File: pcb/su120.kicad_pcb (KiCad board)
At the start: 2 copper layers, 94.1 x 94.1 mm, 293 parts, among them SW1 SW_Push, SW10 SW_Push, SW11 SW_Push, SW12 SW_Push, SW13 SW_Push, SW14 SW_Push, SW15 SW_Push, SW2 SW_Push, SW3 SW_Push, SW4 SW_Push, SW5 SW_Push, SW6 SW_Push, SW7 SW_Push, SW8 SW_Push, SW9 SW_Push

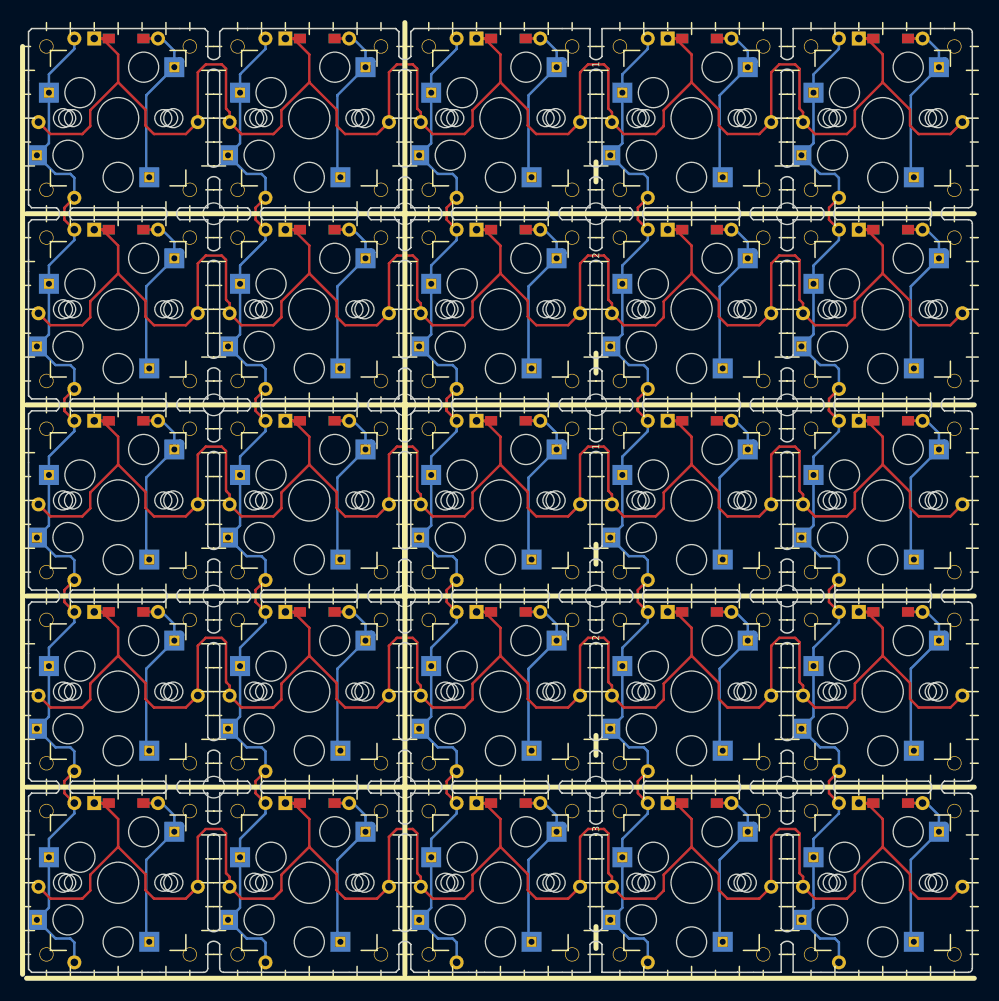
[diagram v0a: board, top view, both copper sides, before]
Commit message: modify to fit choc v2
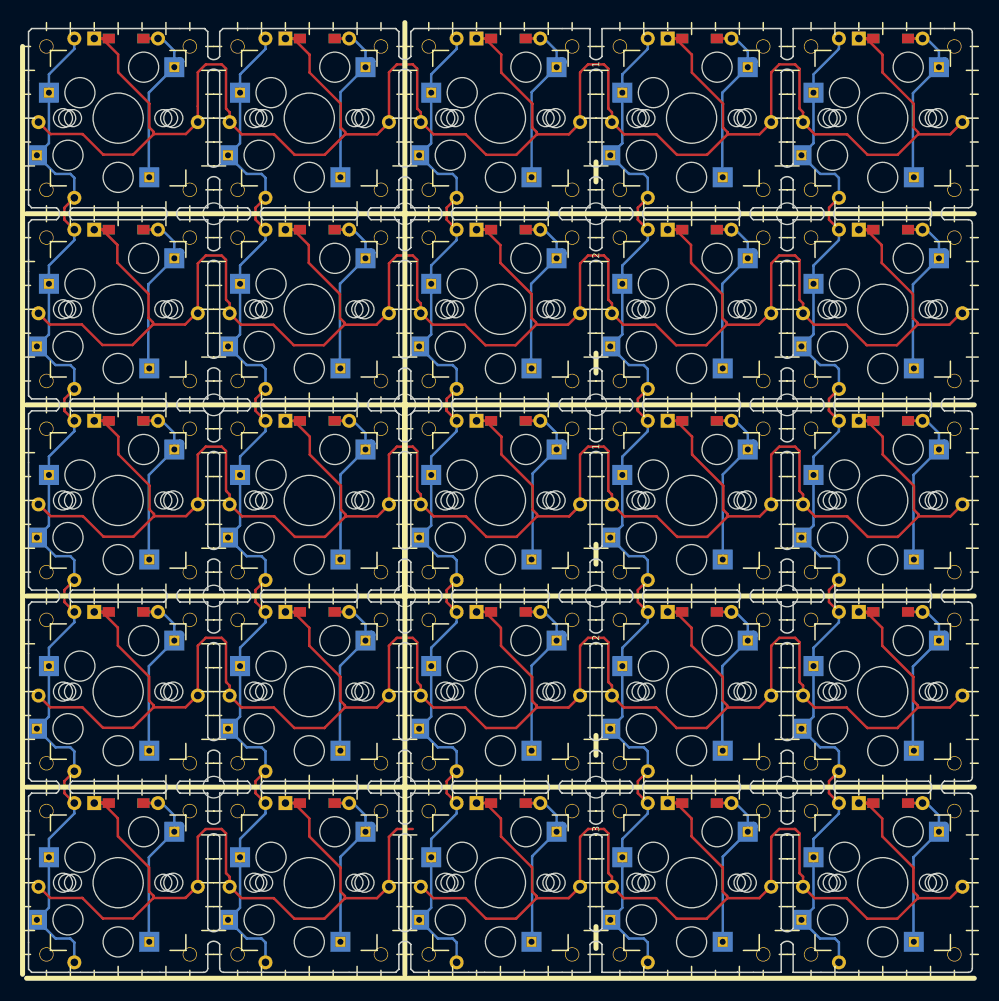
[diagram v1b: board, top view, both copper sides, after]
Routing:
- net Y1: track 417.2 -> 439.1 mm
- net Y2: track 417.2 -> 439.1 mm
- net Y3: track 209.0 -> 213.9 mm
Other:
- net class Default removed
- net class PWR removed
- rule pad_to_mask_clearance: 0.2 -> 0
